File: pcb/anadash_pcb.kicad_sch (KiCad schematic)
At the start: 14 parts

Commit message: Finish up the schematic
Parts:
- added SW1, SW2, SW3, SW4, SW5, SW6, SW7, SW8: SW_Push, Button_Switch_Keyboard:SW_Cherry_MX_1.00u_PCB, symbol Switch:SW_Push
- added U2: ER_OLEDM0.91_1x-I2C, Display:ER_OLEDM0.91_1x-I2C, symbol Display_Graphic:ER_OLEDM0.91_1x-I2C
- J1: renamed from J?; value Meter? -> Meter1; footprint (none) -> Connector_JST:JST_XH_B2B-XH-A_1x02_P2.50mm_Vertical
- J2: renamed from J?; value Meter? -> Meter2; footprint (none) -> Connector_JST:JST_XH_B2B-XH-A_1x02_P2.50mm_Vertical
- J3: renamed from J?; value Meter? -> Meter3; footprint (none) -> Connector_JST:JST_XH_B2B-XH-A_1x02_P2.50mm_Vertical
- J4: renamed from J?; value Meter? -> Meter4; footprint (none) -> Connector_JST:JST_XH_B2B-XH-A_1x02_P2.50mm_Vertical
- R1, R2, R3, R4, R5, R6, R7, R8: renamed from R?; footprint (none) -> Resistor_THT:R_Axial_DIN0207_L6.3mm_D2.5mm_P7.62mm_Horizontal
- U1: renamed from U?; footprint (none) -> Adafruit_MCP4728:Adafruit_MCP4728
- gave numbers to parts that had none: 1
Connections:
- net +3V3: now also U2.2 (VCC)
- net GND: now also SW1.1, SW2.1, SW3.1, SW4.1, SW5.1, SW6.1, SW7.1, SW8.1, U2.1 (GND)
- net SCL: now also U2.3 (SCL)
- net SDA: now also U2.4 (SDA)
- net at A1.10 (GPIO7): now also SW4.2
- net at A1.11 (GPIO8): now also SW5.2
- net at A1.12 (GPIO9): now also SW6.2
- net at A1.14 (GPIO10): now also SW7.2
- net at A1.15 (GPIO11): now also SW8.2
- net at A1.6 (GPIO4): now also SW1.2
- net at A1.7 (GPIO5): now also SW2.2
- net at A1.9 (GPIO6): now also SW3.2
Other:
- note added: "Display"
- note added: "MCU and Switches"
- moved on the sheet: A1, J1, J2, J3, J4, R1, R2, R3, R4, R5, R6, R7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

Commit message: esp32 switch :d
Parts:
- removed A1: RaspberryPi_Pico, Module:RaspberryPi_Pico_Common_Unspecified, symbol MCU_Module:RaspberryPi_Pico
- added BZ1: Buzzer, Buzzer_Beeper:Buzzer_D14mm_H7mm_P10mm, symbol Device:Buzzer
- added SW9: RotaryEncoder, symbol Device:RotaryEncoder
- added U3: ESP32-DevKitC, PCM_Espressif:ESP32-DevKitC, symbol Espressif:ESP32-DevKitC
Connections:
- net +3V3: now also U3.1 (3V3)
- net GND: now also BZ1.2 (-), SW9.C, U3.14 (GND), U3.32 (GND), U3.38 (GND)
- net SCL: now also U3.36 (GPIO22)
- net SDA: now also U3.33 (GPIO21)
- net at SW4.2: now also U3.20 (SD_CLK/GPIO6)
- net at SW5.2: now also U3.21 (SD_DATA0/GPIO7)
- net at SW6.2: now also U3.22 (SD_DATA1/GPIO8)
- net at SW7.2: now also U3.16 (SD_DATA2/GPIO9)
- net at SW8.2: now also U3.17 (SD_DATA3/GPIO10)
- net at SW1.2: now also U3.30 (GPIO18)
- net at SW2.2: now also U3.31 (GPIO19)
- net at SW3.2: now also U3.37 (GPIO23)
- new net: SW9.B, U3.27 (GPIO16)
- new net: SW9.A, U3.28 (GPIO17)
- new net: BZ1.1 (+), U3.29 (GPIO5)
- no-connect marks 0 -> 1
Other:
- title: (none) -> Anadash PCB
- moved on the sheet: SW1, SW2, SW3, SW4, SW5, SW6, SW7, SW8

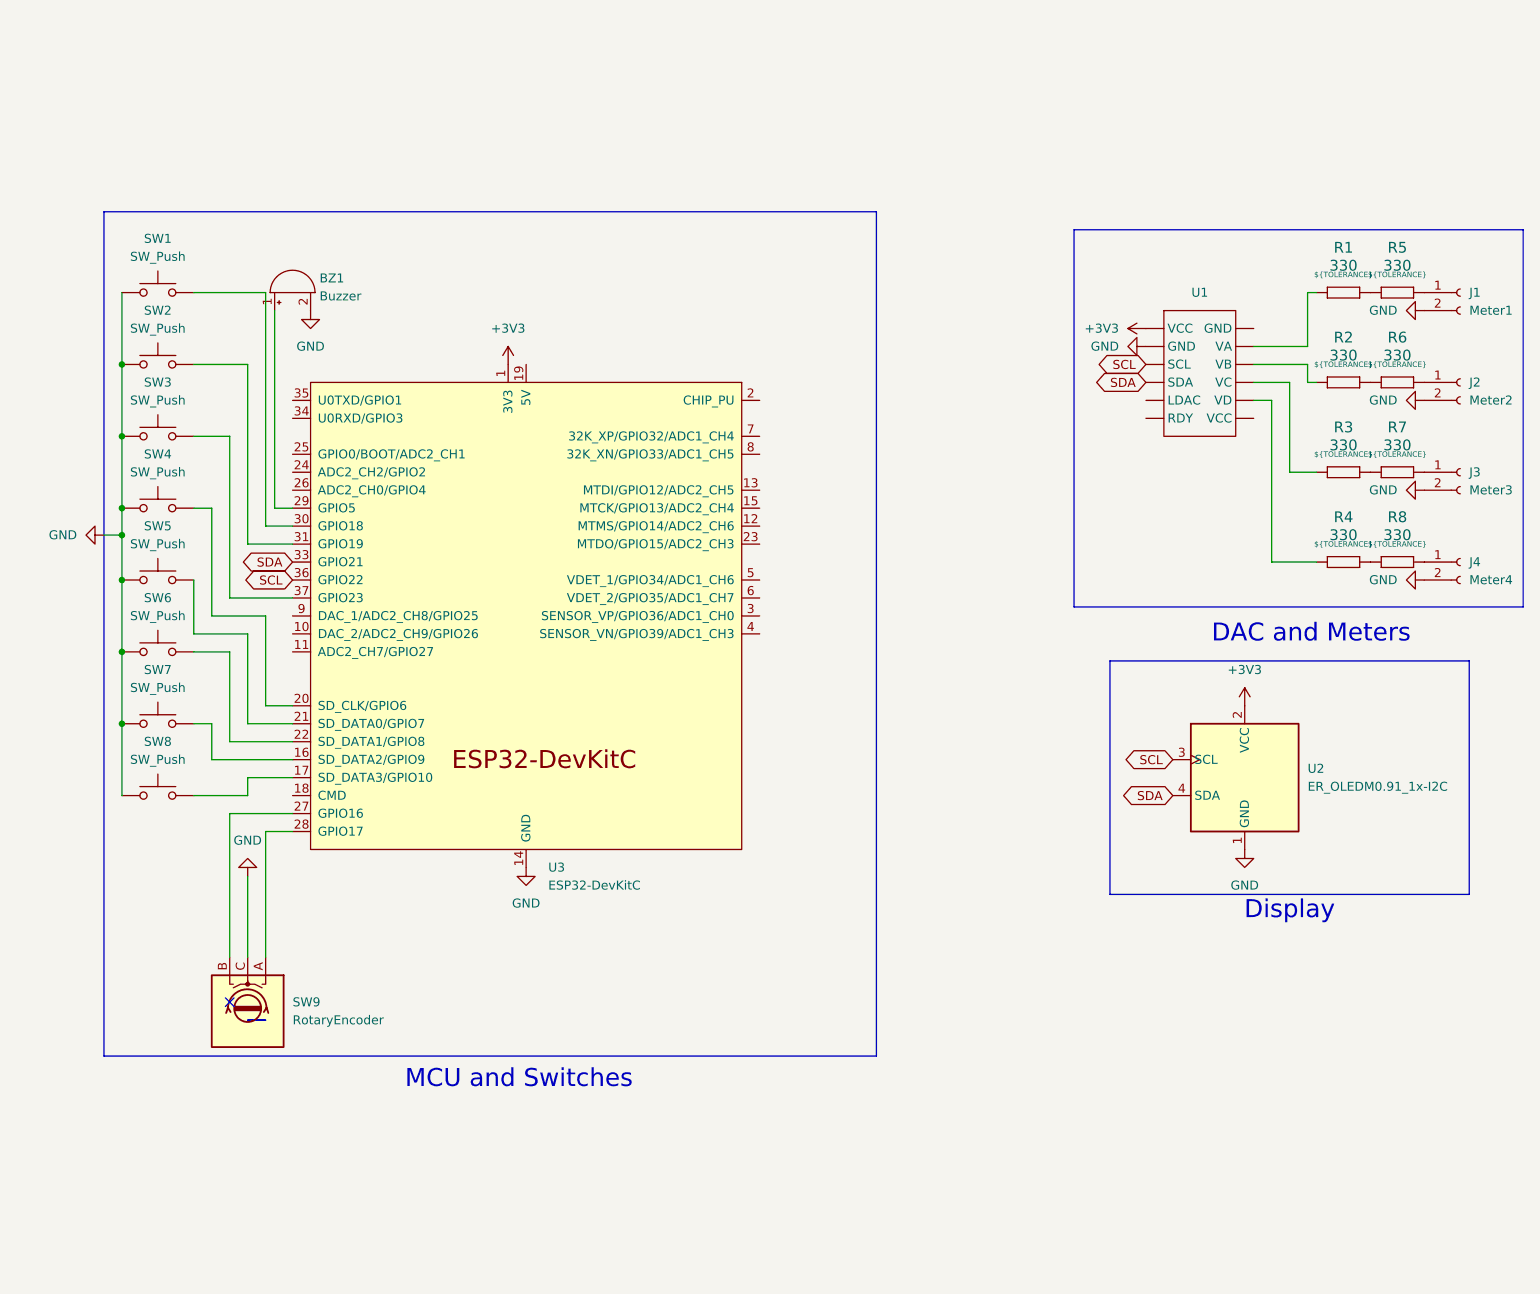
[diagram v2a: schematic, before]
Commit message: Revert "esp32 switch :d"
This reverts commit a7c39a4a50a5a8529a2412f65cccd0cacde0d017.
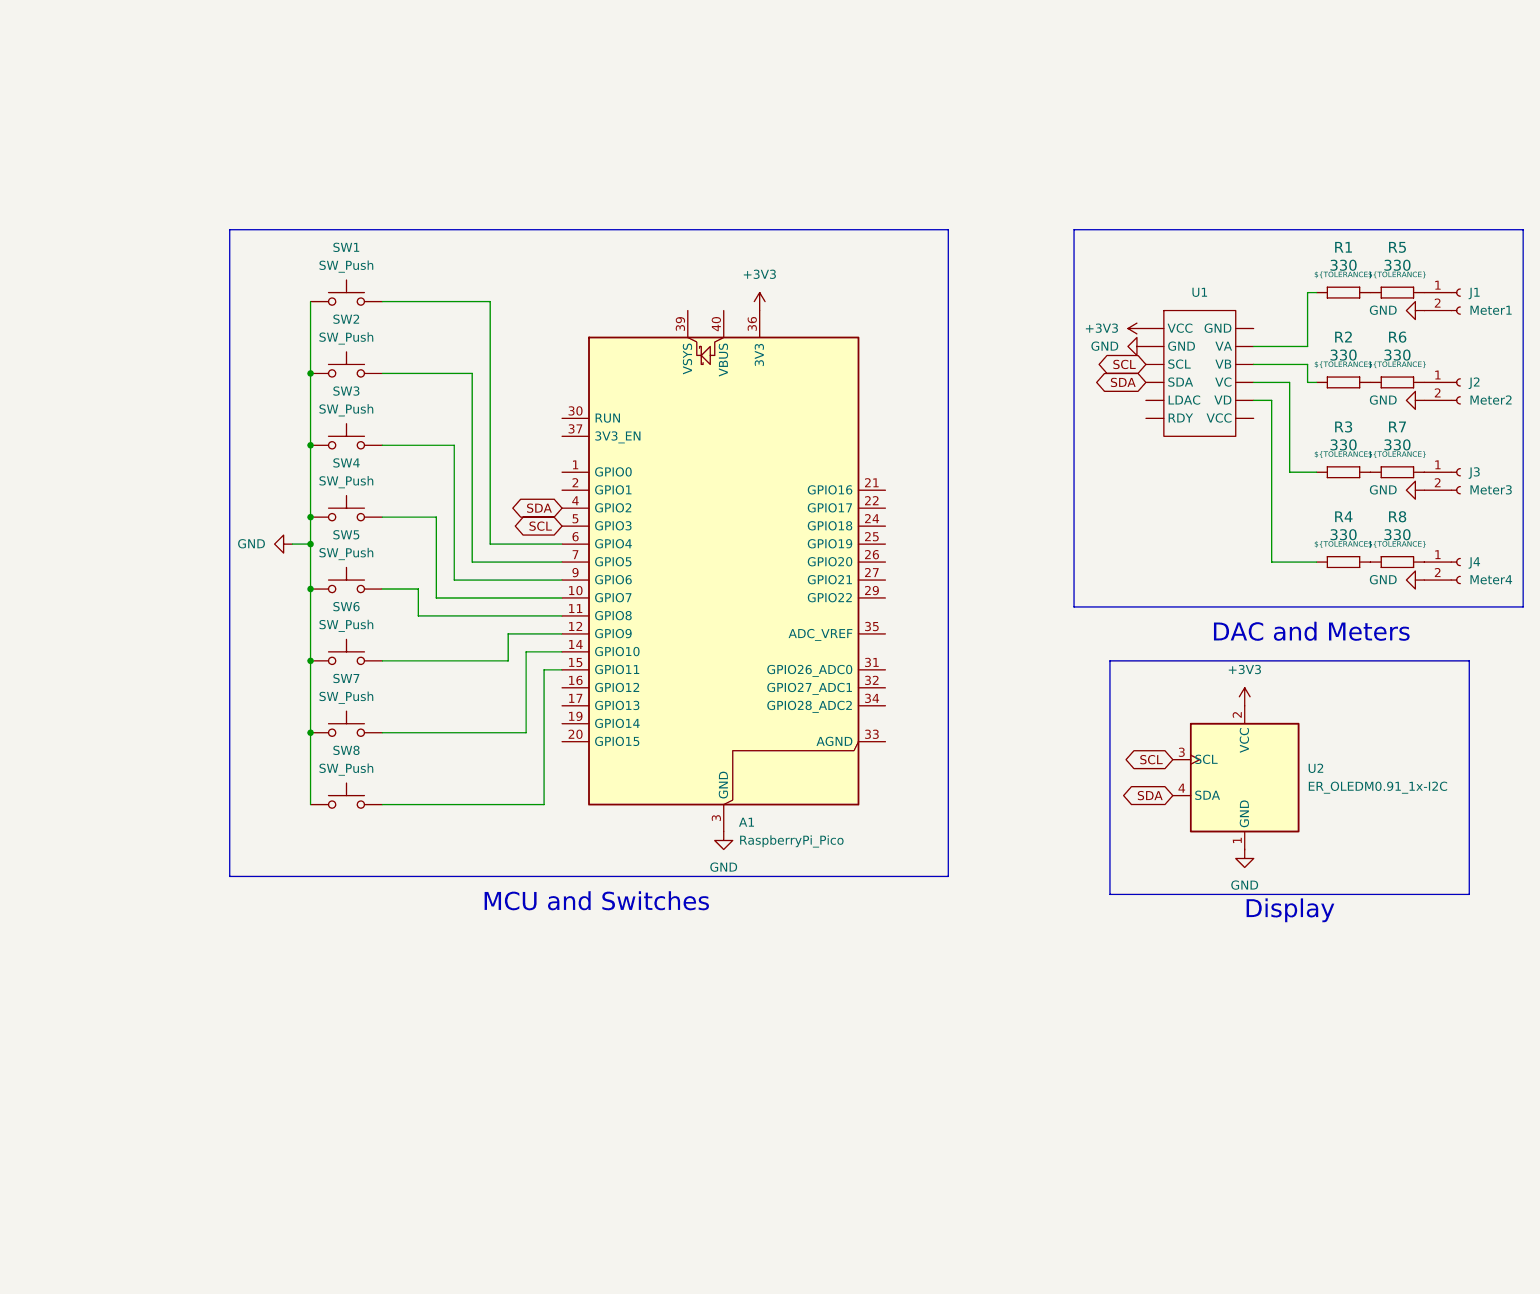
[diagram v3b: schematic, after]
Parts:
- removed BZ1: Buzzer, Buzzer_Beeper:Buzzer_D14mm_H7mm_P10mm, symbol Device:Buzzer
- removed SW9: RotaryEncoder, symbol Device:RotaryEncoder
- removed U3: ESP32-DevKitC, PCM_Espressif:ESP32-DevKitC, symbol Espressif:ESP32-DevKitC
- added A1: RaspberryPi_Pico, Module:RaspberryPi_Pico_Common_Unspecified, symbol MCU_Module:RaspberryPi_Pico
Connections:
- net +3V3: now also A1.36 (3V3)
- net GND: now also A1.13 (GND), A1.18 (GND), A1.23 (GND), A1.28 (GND), A1.3 (GND), A1.38 (GND), A1.8 (GND)
- net SCL: now also A1.5 (GPIO3)
- net SDA: now also A1.4 (GPIO2)
- net at SW5.2: now also A1.11 (GPIO8)
- net at SW7.2: now also A1.14 (GPIO10)
- net at SW8.2: now also A1.15 (GPIO11)
- net at SW4.2: now also A1.10 (GPIO7)
- net at SW6.2: now also A1.12 (GPIO9)
- net at SW1.2: now also A1.6 (GPIO4)
- net at SW2.2: now also A1.7 (GPIO5)
- net at SW3.2: now also A1.9 (GPIO6)
- no-connect marks 1 -> 0
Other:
- title: Anadash PCB -> (none)
- moved on the sheet: SW1, SW2, SW3, SW4, SW5, SW6, SW7, SW8

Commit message: Added test pads, change the switches's wiring, added an encoder
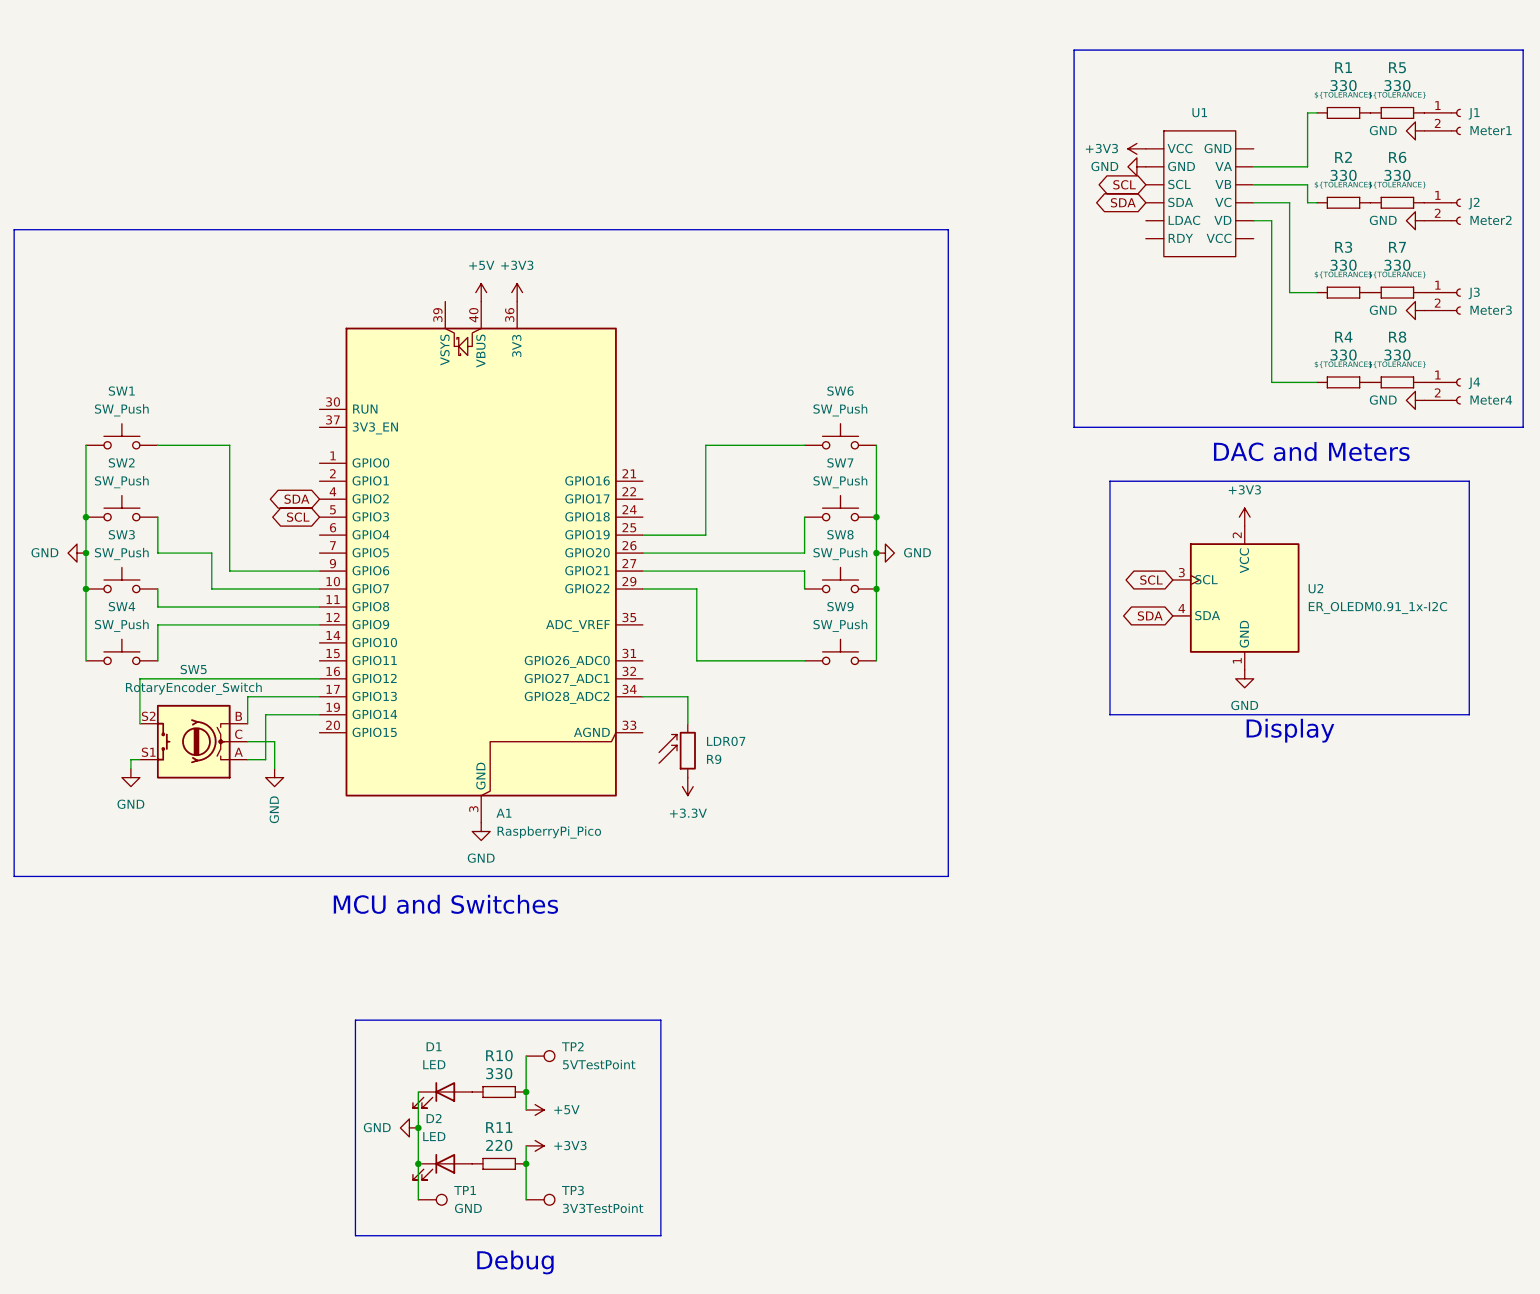
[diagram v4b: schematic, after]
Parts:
- removed SW5: SW_Push, Button_Switch_Keyboard:SW_Cherry_MX_1.00u_PCB, symbol Switch:SW_Push
- added D1, D2: LED, LED_THT:LED_D5.0mm, symbol Device:LED
- added R10: 330, Resistor_THT:R_Axial_DIN0207_L6.3mm_D2.5mm_P7.62mm_Horizontal, symbol Resistors:Resistor
- added R11: 220, Resistor_THT:R_Axial_DIN0207_L6.3mm_D2.5mm_P7.62mm_Horizontal, symbol Resistors:Resistor
- added R9: LDR07, OptoDevice:R_LDR_5.1x4.3mm_P3.4mm_Vertical, symbol Sensor_Optical:LDR07
- added SW5: RotaryEncoder_Switch, Rotary_Encoder:RotaryEncoder_Alps_EC11E-Switch_Vertical_H20mm, symbol Device:RotaryEncoder_Switch
- added SW9: SW_Push, Button_Switch_Keyboard:SW_Cherry_MX_1.00u_PCB, symbol Switch:SW_Push
- added TP1: GND, TestPoint:TestPoint_Pad_D2.0mm, symbol Connector:TestPoint
- added TP2: 5VTestPoint, TestPoint:TestPoint_Pad_D2.0mm, symbol Connector:TestPoint
- added TP3: 3V3TestPoint, TestPoint:TestPoint_Pad_D2.0mm, symbol Connector:TestPoint
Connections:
- net +3V3: now also R11.2, TP3.1
- net GND: now also D1.1 (K), D2.1 (K), SW5.C, SW5.S1, SW9.1, TP1.1
- net at A1.10 (GPIO7): now also SW2.2; no longer SW4.2
- net at A1.11 (GPIO8): now also SW3.2
- net at A1.12 (GPIO9): now also SW4.2; no longer SW6.2
- net at A1.14 (GPIO10): no longer SW7.2
- net at A1.15 (GPIO11): no longer SW8.2
- net at A1.16 (GPIO12): now also SW5.S2
- net at A1.17 (GPIO13): now also SW5.B
- net at A1.19 (GPIO14): now also SW5.A
- net at A1.25 (GPIO19): now also SW6.2
- net at A1.26 (GPIO20): now also SW7.2
- net at A1.27 (GPIO21): now also SW8.2
- net at A1.29 (GPIO22): now also SW9.2
- net at A1.34 (GPIO28_ADC2): now also R9.2
- net +5V: now reaches A1.40 (VBUS)
- net +5V: now also R10.2, TP2.1
- net at A1.6 (GPIO4): no longer SW1.2
- net at A1.7 (GPIO5): no longer SW2.2
- net at A1.9 (GPIO6): now also SW1.2; no longer SW3.2
- new net: D2.2 (A), R11.1
- new net: D1.2 (A), R10.1
- new net +3.3V: R9.1
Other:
- note added: "Debug"
- moved on the sheet: A1, J1, J2, J3, J4, R1, R2, R3, R4, R5, R6, R7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
